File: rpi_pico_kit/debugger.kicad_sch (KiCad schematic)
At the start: 39 parts, among them J3 USB_B, U2 RP2040, U3 NCP1117-3.3_SOT223, U4 W25Q16JVSSIQ, Y1 12MHz

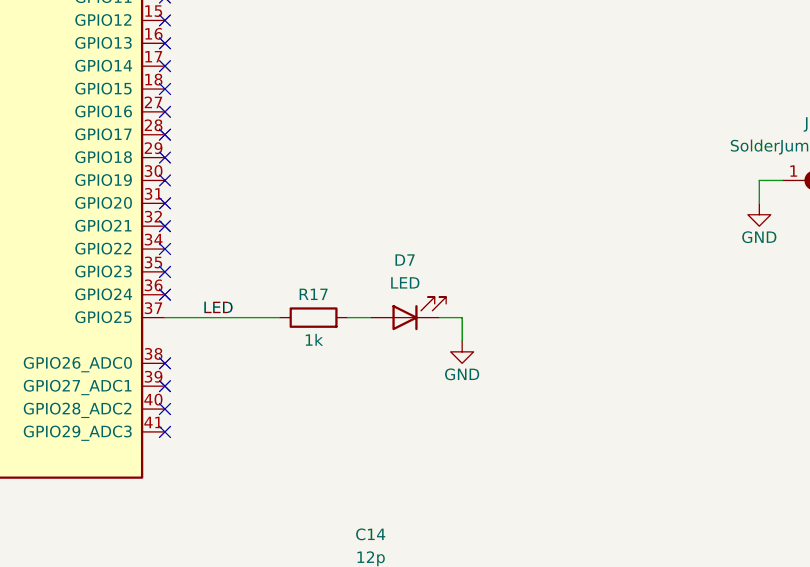
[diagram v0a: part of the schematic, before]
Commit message: added another MPNs, edited color of LEDs
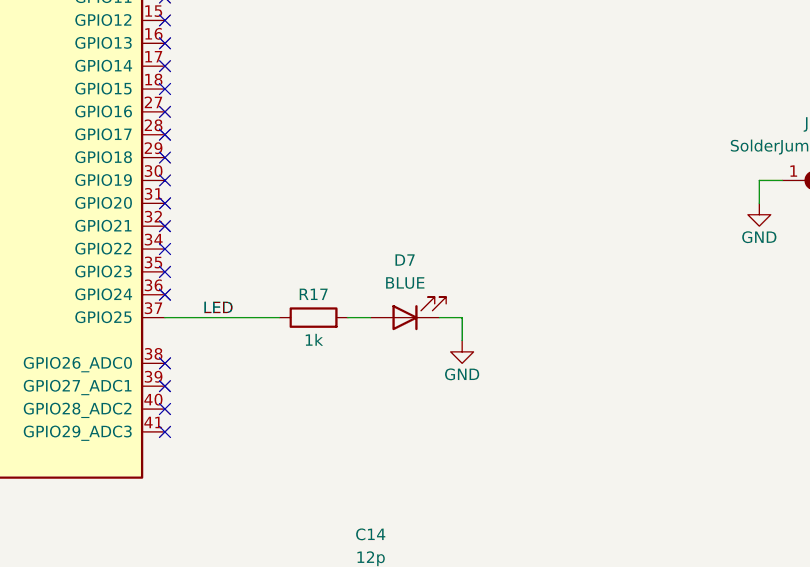
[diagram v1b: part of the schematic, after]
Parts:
- D7: value LED -> BLUE
- U2: Manufacturer Part Number (none) -> SC0914(13); Supplier (none) -> Digikey; Supplier Part URL (none) -> https://www.digikey.cz/en/products/detail/raspberry-pi/SC09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
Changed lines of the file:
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@@
       (effects (font (size 1.27 1.27)) hide)
     )
-    (property "Datasheet" "" (id 3) (at 58.42 110.49 0)
+    (property "Datasheet" "~" (id 3) (at 58.42 110.49 0)
+      (effects (font (size 1.27 1.27)) hide)
+    )
+    (property "Manufacturer Part Number" "SC0914(13)" (id 4) (at 77.47 110.49 0)
+      (effects (font (size 1.27 1.27)) hide)
+    )
+    (property "Supplier" "Digikey" (id 5) (at 77.47 110.49 0)
+      (effects (font (size 1.27 1.27)) hide)
+    )
+    (property "Supplier Part URL" "https://www.digikey.cz/en/products/detail/raspberry-pi/SC0914-13/14306010" (id 6) (at 77.47 110.49 0)
       (effects (font (size 1.27 1.27)) hide)
     )
@@
       (effects (font (size 1.27 1.27)) hide)
     )
-    (property "Datasheet" " ~" (id 3) (at 201.93 46.99 0)
+    (property "Datasheet" "~" (id 3) (at 201.93 46.99 0)
       (effects (font (size 1.27 1.27)) hide)
     )
@@
       (effects (font (size 1.27 1.27)))
     )
-    (property "Value" "LED" (id 1) (at 135.89 137.16 0)
+    (property "Value" "BLUE" (id 1) (at 135.89 137.16 0)
       (effects (font (size 1.27 1.27)))
     )
@@
       (effects (font (size 1.27 1.27)) hide)
     )
-    (property "Datasheet" "" (id 3) (at 237.49 128.27 0)
-      (effects (font (size 1.27 1.27)) hide)
-    )
+    (property "Datasheet" "~" (id 3) (at 237.49 128.27 0)
+      (effects (font (size 1.27 1.27)) hide)
+    )

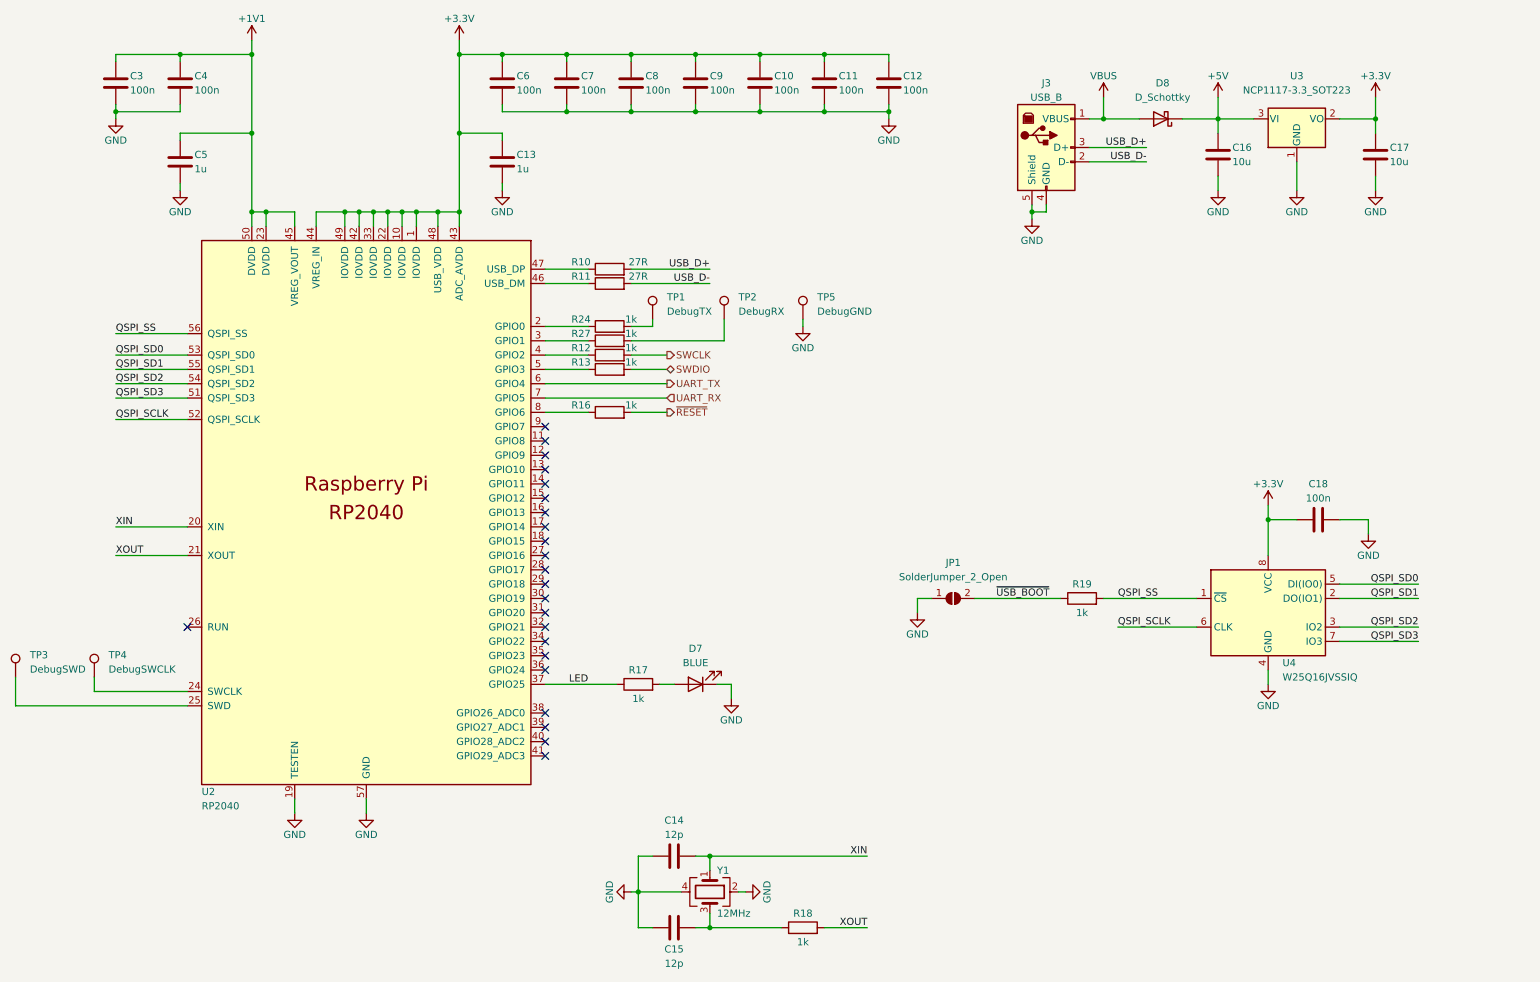
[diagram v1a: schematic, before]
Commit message: added monostable for debug led
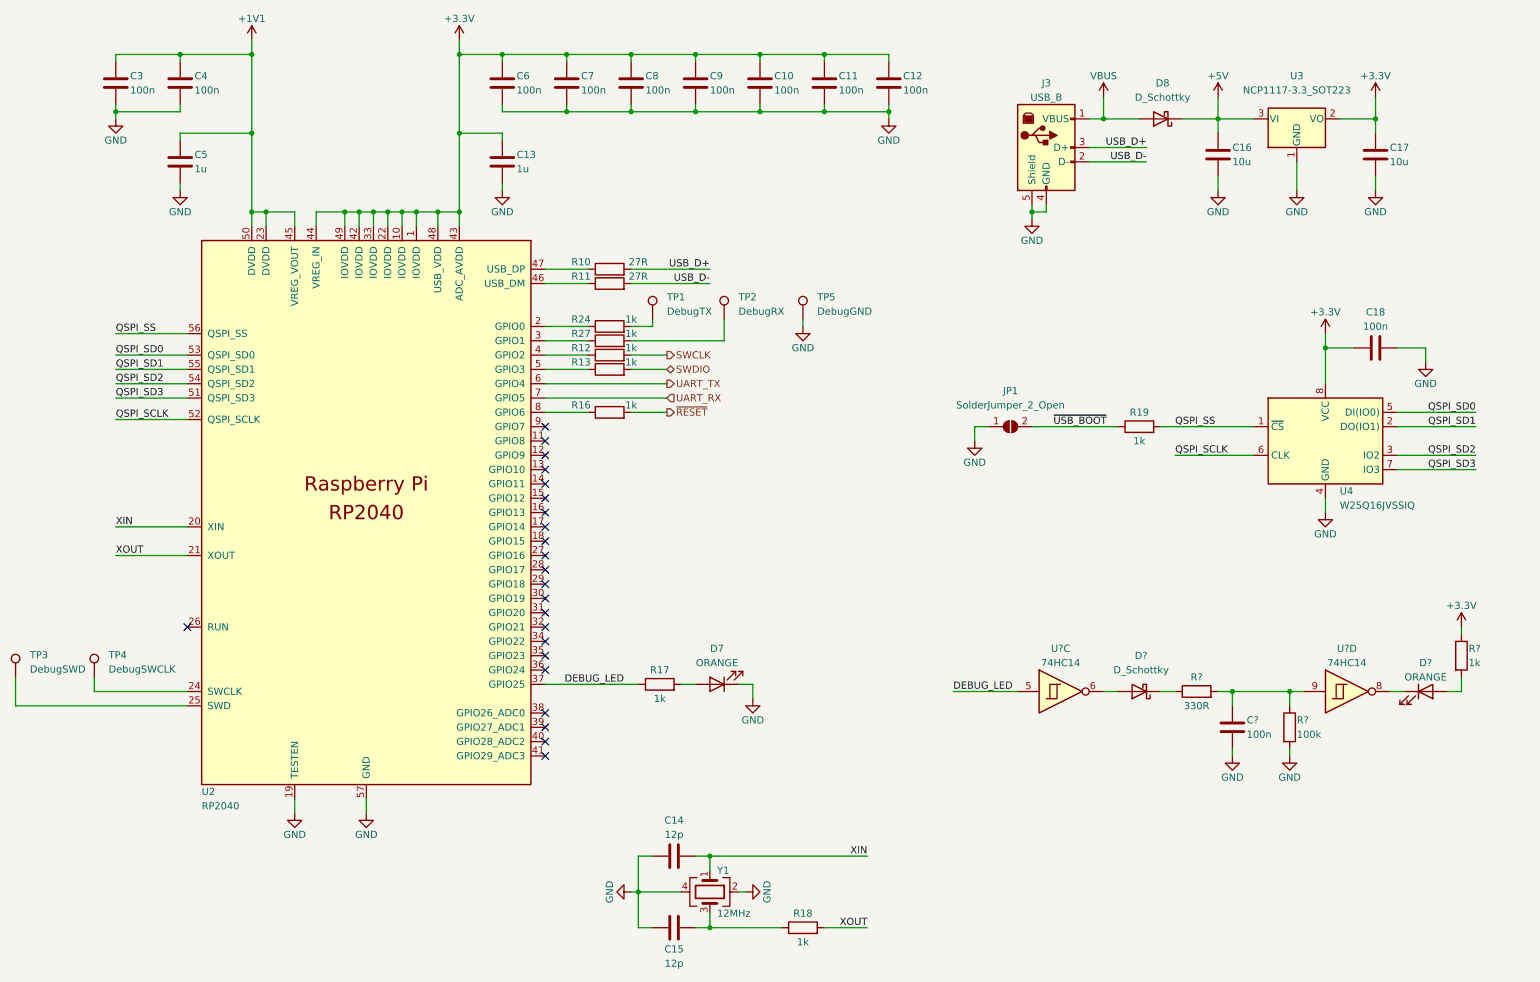
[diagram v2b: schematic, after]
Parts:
- added C?: 100n, Capacitor_SMD:C_0805_2012Metric_Pad1.18x1.45mm_HandSolder, symbol Device:C
- added D?: D_Schottky, Diode_SMD:D_SMB, symbol Device:D_Schottky
- added D?: ORANGE, LED_SMD:LED_0805_2012Metric_Pad1.15x1.40mm_HandSolder, symbol Device:LED
- added R?: 100k, Resistor_SMD:R_0805_2012Metric_Pad1.20x1.40mm_HandSolder, symbol Device:R
- added R?: 330R, Resistor_SMD:R_0805_2012Metric_Pad1.20x1.40mm_HandSolder, symbol Device:R
- added R?: 1k, Resistor_SMD:R_0805_2012Metric_Pad1.20x1.40mm_HandSolder, symbol Device:R
- added U? (x2): 74HC14, Package_SO:SOIC-14_3.9x8.7mm_P1.27mm, symbol 74xx:74HC14
- D7: value BLUE -> ORANGE
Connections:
- net +3V3: now also R?.1
- net GND: now also C?.1, R?.2
- net LED renamed DEBUG_LED
- net DEBUG_LED: now also U?.5
- new net: C?.2, R?.1, R?.2, U?.9
- new net: D?.1 (K), R?.1
- new net: D?.2 (A), R?.2
- new net: D?.2 (A), U?.6
- new net: D?.1 (K), U?.8
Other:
- moved on the sheet: C18, D7, JP1, R17, R19, U4

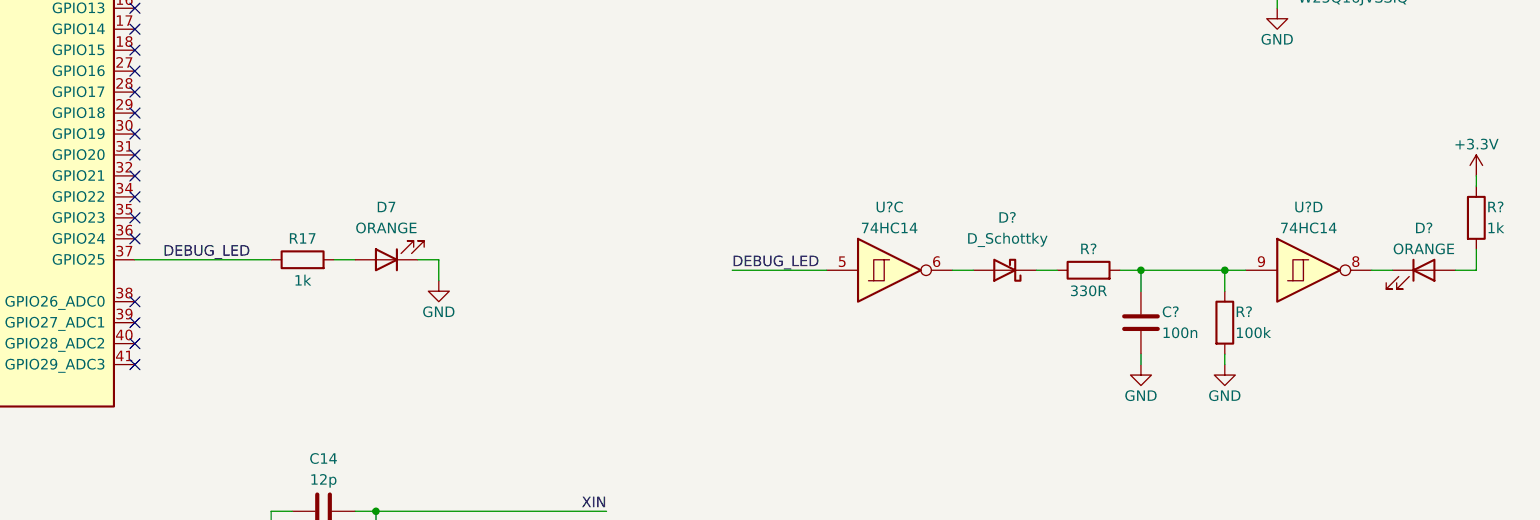
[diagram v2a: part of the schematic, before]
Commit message: changed back 7414 gates to mosfets
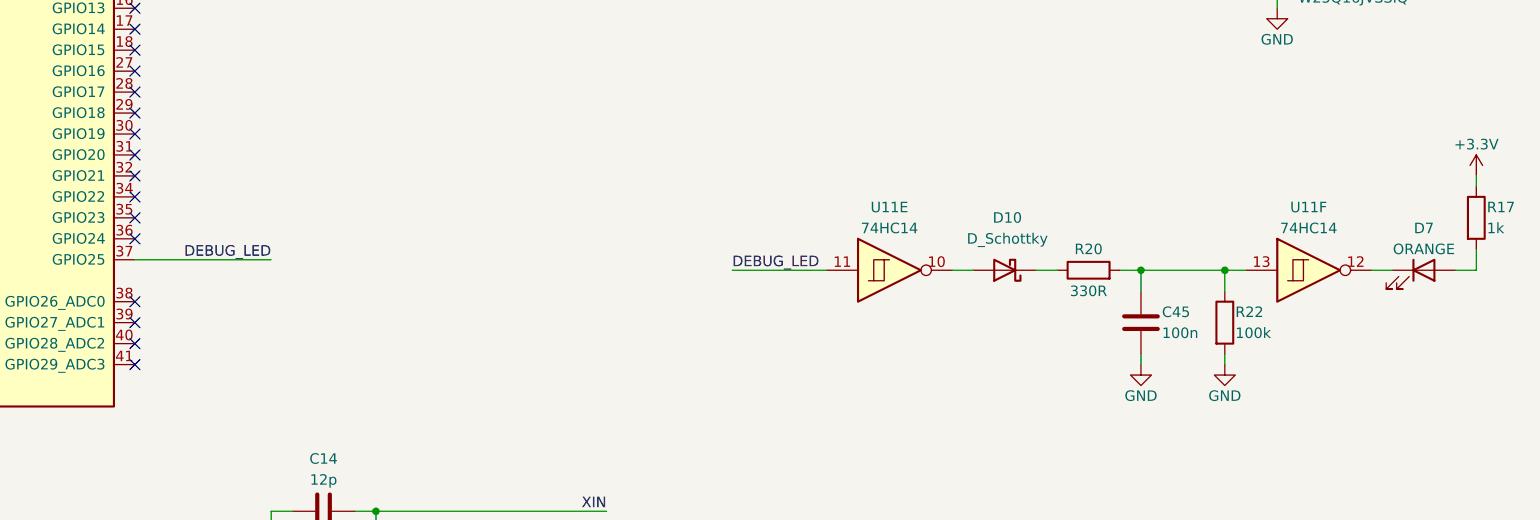
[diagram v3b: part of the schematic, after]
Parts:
- removed D7: ORANGE, LED_SMD:LED_0805_2012Metric_Pad1.15x1.40mm_HandSolder, symbol Device:LED
- removed R17: 1k, Resistor_SMD:R_0805_2012Metric_Pad1.20x1.40mm_HandSolder, symbol Device:R
- gave numbers to parts that had none: 7
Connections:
- net DEBUG_LED: now also U11.11; no longer U11.5
- net at C45.2, R20.2, R22.1: now also U11.13; no longer U11.9
- net at D10.2 (A): now also U11.10; no longer U11.6
- net at D7.1 (K): now also U11.12; no longer U11.8
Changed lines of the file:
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@@
-    (stroke (width 0) (type default))
-  )
-  (wire (pts (xy 143.51 140.97) (xy 146.05 140.97))
     (stroke (width 0) (type default))
   )
@@
     (stroke (width 0) (type default))
   )
-  (wire (pts (xy 146.05 140.97) (xy 146.05 143.51))
-    (stroke (width 0) (type default))
-  )
   (wire (pts (xy 265.43 81.28) (xy 265.43 83.82))
     (stroke (width 0) (type default))
@@
   )
   (wire (pts (xy 109.22 80.01) (xy 116.84 80.01))
-    (stroke (width 0) (type default))
-  )
-  (wire (pts (xy 133.35 140.97) (xy 135.89 140.97))
     (stroke (width 0) (type default))
   )
@@
     (effects (font (size 1.27 1.27)) (justify left bottom))
   )
-  (label "DEBUG_LED" (at 123.19 140.97 0) (fields_autoplaced)
+  (label "DEBUG_LED" (at 125.73 140.97 0) (fields_autoplaced)
     (effects (font (size 1.27 1.27)) (justify right bottom))
   )
@@
   (symbol (lib_id "Device:C") (at 231.14 148.59 180) (unit 1)
     (in_bom yes) (on_board yes)
-    (property "Reference" "C?" (id 0) (at 233.68 147.32 0)
+    (property "Reference" "C45" (id 0) (at 233.68 147.32 0)
       (effects (font (size 1.27 1.27)) (justify right))
     )
@@
   (symbol (lib_id "power:GND") (at 231.14 153.67 0) (unit 1)
     (in_bom yes) (on_board yes)
-    (property "Reference" "#PWR?" (id 0) (at 231.14 160.02 0)
+    (property "Reference" "#PWR05" (id 0) (at 231.14 160.02 0)
       (effects (font (size 1.27 1.27)) hide)
     )
@@
     (pin "2")
   )
-  (symbol (lib_id "power:GND") (at 146.05 143.51 0) (unit 1)
-    (in_bom yes) (on_board yes)
-    (property "Reference" "#PWR024" (id 0) (at 146.05 149.86 0)
-      (effects (font (size 1.27 1.27)) hide)
-    )
-    (property "Value" "GND" (id 1) (at 146.05 147.32 0)
-      (effects (font (size 1.27 1.27)))
-    )
-    (property "Footprint" "" (id 2) (at 146.05 143.51 0)
-      (effects (font (size 1.27 1.27)) hide)
-    )
-    (property "Datasheet" "" (id 3) (at 146.05 143.51 0)
-      (effects (font (size 1.27 1.27)) hide)
-    )
-    (pin "1")
-  )
   (symbol (lib_id "Device:R") (at 241.3 148.59 0) (unit 1)
     (in_bom yes) (on_board yes)
-    (property "Reference" "R?" (id 0) (at 242.57 147.32 0)
+    (property "Reference" "R22" (id 0) (at 242.57 147.32 0)
       (effects (font (size 1.27 1.27)) (justify left))
     )
@@
     )
     (property "Supplier" "Digikey" (id 6) (at 241.3 148.59 0)
-      (effects (font (size 1.27 1.27)) hide)
-    )
-    (pin "1")
-    (pin "2")
-  )
-  (symbol (lib_id "Device:R") (at 129.54 140.97 90) (unit 1)
-    (in_bom yes) (on_board yes)
-    (property "Reference" "R17" (id 0) (at 129.54 138.43 90)
-      (effects (font (size 1.27 1.27)))
-    )
-    (property "Value" "1k" (id 1) (at 129.54 143.51 90)
-      (effects (font (size 1.27 1.27)))
-    )
-    (property "Footprint" "Resistor_SMD:R_0805_2012Metric_Pad1.20x1.40mm_HandSolder" (id 2) (at 129.54 142.748 90)
-      (effects (font (size 1.27 1.27)) hide)
-    )
-    (property "Datasheet" "~" (id 3) (at 129.54 140.97 0)
-      (effects (font (size 1.27 1.27)) hide)
-    )
-    (property "Manufacturer Part Number" "RC0805FR-071KL" (id 4) (at 129.54 140.97 0)
-      (effects (font (size 1.27 1.27)) hide)
-    )
-    (property "Supplier Part URL" "https://www.digikey.cz/en/products/detail/yageo/RC0805FR-071KL/727444" (id 5) (at 129.54 140.97 0)
-      (effects (font (size 1.27 1.27)) hide)
-    )
-    (property "Supplier" "Digikey" (id 6) (at 129.54 140.97 0)
       (effects (font (size 1.27 1.27)) hide)
     )
@@
   (symbol (lib_id "Device:R") (at 224.79 142.24 90) (unit 1)
     (in_bom yes) (on_board yes)
-    (property "Reference" "R?" (id 0) (at 224.79 139.7 90)
+    (property "Reference" "R20" (id 0) (at 224.79 139.7 90)
       (effects (font (size 1.27 1.27)))
     )
@@
   (symbol (lib_id "Device:R") (at 271.78 135.89 0) (unit 1)
     (in_bom yes) (on_board yes)
-    (property "Reference" "R?" (id 0) (at 273.05 134.62 0)
+    (property "Reference" "R17" (id 0) (at 273.05 134.62 0)
       (effects (font (size 1.27 1.27)) (justify left))
     )
@@
     (pin "2")
   )
-  (symbol (lib_id "Device:LED") (at 139.7 140.97 180) (unit 1)
-    (in_bom yes) (on_board yes)
-    (property "Reference" "D7" (id 0) (at 139.7 134.62 0)
-      (effects (font (size 1.27 1.27)))
-    )
-    (property "Value" "ORANGE" (id 1) (at 139.7 137.16 0)
-      (effects (font (size 1.27 1.27)))
-    )
-    (property "Footprint" "LED_SMD:LED_0805_2012Metric_Pad1.15x1.40mm_HandSolder" (id 2) (at 139.7 140.97 0)
-      (effects (font (size 1.27 1.27)) hide)
-    )
-    (property "Datasheet" "~" (id 3) (at 139.7 140.97 0)
-      (effects (font (size 1.27 1.27)) hide)
-    )
-    (pin "1")
-    (pin "2")
-  )
   (symbol (lib_id "Device:C") (at 256.54 46.99 180) (unit 1)
     (in_bom yes) (on_board yes)
@@
   (symbol (lib_id "Device:D_Schottky") (at 214.63 142.24 180) (unit 1)
     (in_bom yes) (on_board yes) (fields_autoplaced)
-    (property "Reference" "D?" (id 0) (at 214.9475 135.89 0)
+    (property "Reference" "D10" (id 0) (at 214.9475 135.89 0)
       (effects (font (size 1.27 1.27)))
     )
@@
     (pin "2")
   )
-  (symbol (lib_id "74xx:74HC14") (at 251.46 142.24 0) (unit 4)
+  (symbol (lib_id "74xx:74HC14") (at 251.46 142.24 0) (unit 6)
     (in_bom yes) (on_board yes) (fields_autoplaced)
-    (property "Reference" "U?" (id 0) (at 251.46 134.62 0)
+    (property "Reference" "U11" (id 0) (at 251.46 134.62 0)
       (effects (font (size 1.27 1.27)))
     )
@@
       (effects (font (size 1.27 1.27)) hide)
     )
-    (pin "8")
-    (pin "9")
+    (pin "12")
+    (pin "13")
   )
   (symbol (lib_id "power:GND") (at 241.3 153.67 0) (unit 1)
     (in_bom yes) (on_board yes)
-    (property "Reference" "#PWR?" (id 0) (at 241.3 160.02 0)
+    (property "Reference" "#PWR06" (id 0) (at 241.3 160.02 0)
       (effects (font (size 1.27 1.27)) hide)
     )
@@
   (symbol (lib_id "power:+3.3V") (at 271.78 130.81 0) (unit 1)
     (in_bom yes) (on_board yes)
-    (property "Reference" "#PWR?" (id 0) (at 271.78 134.62 0)
+    (property "Reference" "#PWR012" (id 0) (at 271.78 134.62 0)
       (effects (font (size 1.27 1.27)) hide)
     )
@@
   (symbol (lib_id "Device:LED") (at 265.43 142.24 0) (unit 1)
     (in_bom yes) (on_board yes)
-    (property "Reference" "D?" (id 0) (at 265.43 137.16 0)
+    (property "Reference" "D7" (id 0) (at 265.43 137.16 0)
       (effects (font (size 1.27 1.27)))
     )
@@
     (pin "2")
   )
-  (symbol (lib_id "74xx:74HC14") (at 200.66 142.24 0) (unit 3)
+  (symbol (lib_id "74xx:74HC14") (at 200.66 142.24 0) (unit 5)
     (in_bom yes) (on_board yes) (fields_autoplaced)
-    (property "Reference" "U?" (id 0) (at 200.66 134.62 0)
+    (property "Reference" "U11" (id 0) (at 200.66 134.62 0)
       (effects (font (size 1.27 1.27)))
     )
@@
       (effects (font (size 1.27 1.27)) hide)
     )
-    (pin "5")
-    (pin "6")
+    (pin "10")
+    (pin "11")
   )
   (symbol (lib_id "Device:C") (at 101.6 48.26 180) (unit 1)

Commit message: changed name of LEDs from D to LED
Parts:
- renumbered D7 to LED4
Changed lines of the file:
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@@
   (symbol (lib_id "Device:LED") (at 265.43 142.24 0) (unit 1)
     (in_bom yes) (on_board yes)
-    (property "Reference" "D7" (id 0) (at 265.43 137.16 0)
+    (property "Reference" "LED4" (id 0) (at 265.43 137.16 0)
       (effects (font (size 1.27 1.27)))
     )
